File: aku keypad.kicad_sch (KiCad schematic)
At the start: 19 parts, among them J1 USB_C_Receptacle_USB2.0, SW1 SW_Push, SW2 MX_SW_HS, SW3 MX_SW_HS, U1 SRV05-4, U2 ATmega32U2-M, Y1 Crystal_GND24_Small

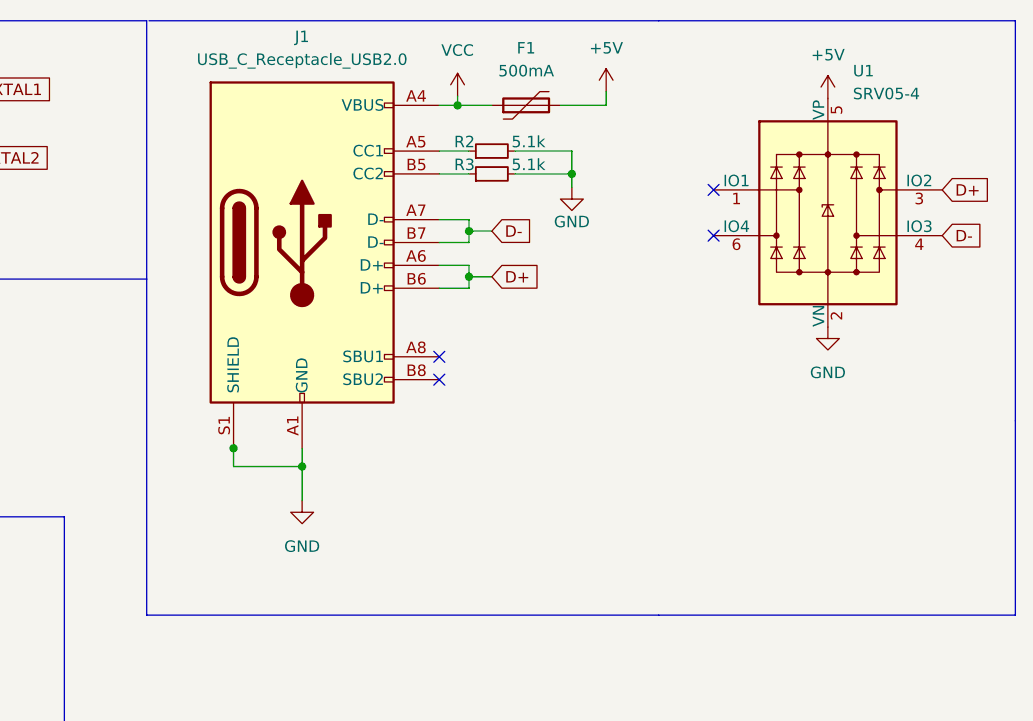
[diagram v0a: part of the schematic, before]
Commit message: redid routing on pcb
added type-c submodule, redid routing, changed usb components
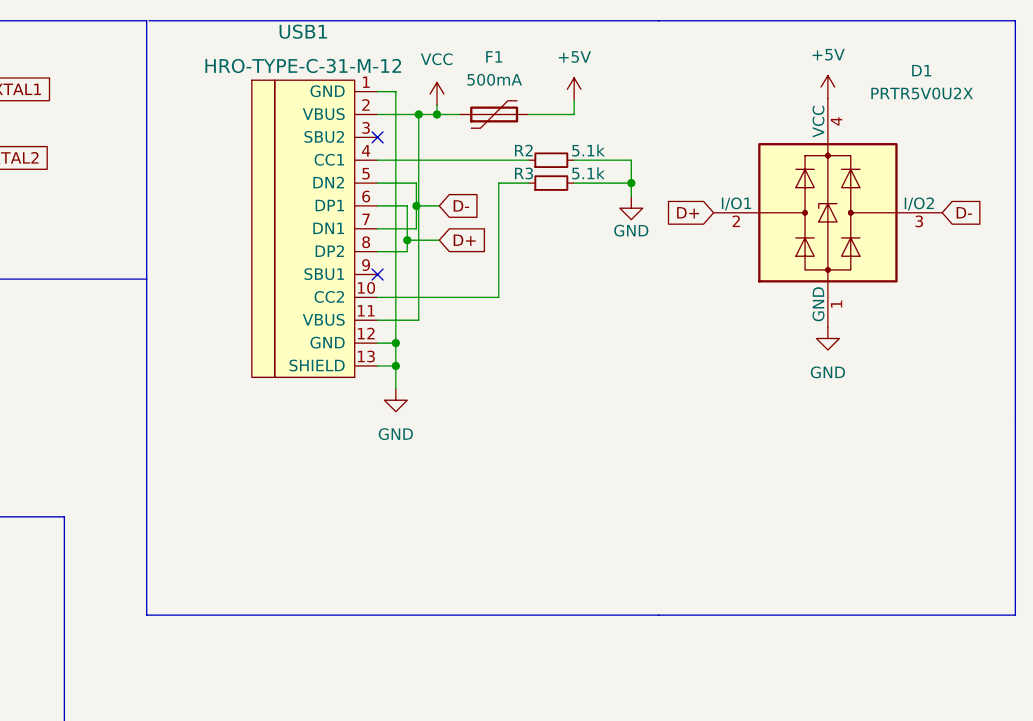
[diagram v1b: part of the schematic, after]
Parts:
- removed J1: USB_C_Receptacle_USB2.0, Connector_USB:USB_C_Receptacle_HRO_TYPE-C-31-M-12, symbol Connector:USB_C_Receptacle_USB2.0
- removed U1: SRV05-4, marbastlib-various:SOT-23-6-routable, symbol marbastlib-various:SRV05-4
- added D1: PRTR5V0U2X, Package_TO_SOT_SMD:SOT-143, symbol Power_Protection:PRTR5V0U2X
- added USB1: HRO-TYPE-C-31-M-12, Type-C:HRO-TYPE-C-31-M-12-HandSoldering, symbol Type-C:HRO-TYPE-C-31-M-12
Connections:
- net +5V: now also D1.4 (VCC)
- net D+: now also D1.2 (I/O1), USB1.6 (DP1), USB1.8 (DP2)
- net D-: now also D1.3 (I/O2), USB1.5 (DN2), USB1.7 (DN1)
- net GND: now also D1.1 (GND), USB1.1 (GND), USB1.12 (GND), USB1.13 (SHIELD)
- net VCC: now also USB1.11 (VBUS), USB1.2 (VBUS)
- net at R3.1: now also USB1.10 (CC2)
- net at R2.1: now also USB1.4 (CC1)
- no-connect marks 4 -> 2
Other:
- moved on the sheet: F1, R2, R3

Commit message: Added mounting holes
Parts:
- added H1, H2, H3, H4: MountingHole, random-keyboard-parts:Generic-Mounthole, symbol Mechanical:MountingHole
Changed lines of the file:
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@@
     (pin "2")
+  )
+  (symbol (lib_id "Mechanical:MountingHole") (at 213.106 103.886 0) (unit 1)
+    (in_bom yes) (on_board yes) (fields_autoplaced)
+    (property "Reference" "H1" (id 0) (at 215.9 102.6159 0)
+      (effects (font (size 1.27 1.27)) (justify left))
+    )
+    (property "Value" "MountingHole" (id 1) (at 215.9 105.1559 0)
+      (effects (font (size 1.27 1.27)) (justify left))
+    )
+    (property "Footprint" "random-keyboard-parts:Generic-Mounthole" (id 2) (at 213.106 103.886 0)
+      (effects (font (size 1.27 1.27)) hide)
+    )
+    (property "Datasheet" "~" (id 3) (at 213.106 103.886 0)
+      (effects (font (size 1.27 1.27)) hide)
+    )
   )
   (symbol (lib_id "Power_Protection:PRTR5V0U2X") (at 247.396 43.942 0) (unit 1)
@@
     (pin "1")
   )
+  (symbol (lib_id "Mechanical:MountingHole") (at 194.564 104.14 0) (unit 1)
+    (in_bom yes) (on_board yes) (fields_autoplaced)
+    (property "Reference" "H3" (id 0) (at 197.358 102.8699 0)
+      (effects (font (size 1.27 1.27)) (justify left))
+    )
+    (property "Value" "MountingHole" (id 1) (at 197.358 105.4099 0)
+      (effects (font (size 1.27 1.27)) (justify left))
+    )
+    (property "Footprint" "random-keyboard-parts:Generic-Mounthole" (id 2) (at 194.564 104.14 0)
+      (effects (font (size 1.27 1.27)) hide)
+    )
+    (property "Datasheet" "~" (id 3) (at 194.564 104.14 0)
+      (effects (font (size 1.27 1.27)) hide)
+    )
+  )
   (symbol (lib_id "Device:R_Small") (at 216.662 40.64 90) (unit 1)
     (in_bom yes) (on_board yes)
@@
     (pin "1")
     (pin "2")
+  )
+  (symbol (lib_id "Mechanical:MountingHole") (at 231.394 103.886 0) (unit 1)
+    (in_bom yes) (on_board yes) (fields_autoplaced)
+    (property "Reference" "H2" (id 0) (at 234.188 102.6159 0)
+      (effects (font (size 1.27 1.27)) (justify left))
+    )
+    (property "Value" "MountingHole" (id 1) (at 234.188 105.1559 0)
+      (effects (font (size 1.27 1.27)) (justify left))
+    )
+    (property "Footprint" "random-keyboard-parts:Generic-Mounthole" (id 2) (at 231.394 103.886 0)
+      (effects (font (size 1.27 1.27)) hide)
+    )
+    (property "Datasheet" "~" (id 3) (at 231.394 103.886 0)
+      (effects (font (size 1.27 1.27)) hide)
+    )
   )
   (symbol (lib_id "Device:C_Small") (at 127.762 37.846 90) (unit 1)
@@
     (pin "1")
   )
+  (symbol (lib_id "Mechanical:MountingHole") (at 175.006 104.648 0) (unit 1)
+    (in_bom yes) (on_board yes) (fields_autoplaced)
+    (property "Reference" "H4" (id 0) (at 177.8 103.3779 0)
+      (effects (font (size 1.27 1.27)) (justify left))
+    )
+    (property "Value" "MountingHole" (id 1) (at 177.8 105.9179 0)
+      (effects (font (size 1.27 1.27)) (justify left))
+    )
+    (property "Footprint" "random-keyboard-parts:Generic-Mounthole" (id 2) (at 175.006 104.648 0)
+      (effects (font (size 1.27 1.27)) hide)
+    )
+    (property "Datasheet" "~" (id 3) (at 175.006 104.648 0)
+      (effects (font (size 1.27 1.27)) hide)
+    )
+  )
   (symbol (lib_id "Device:R_Small") (at 40.132 34.036 0) (unit 1)
     (in_bom yes) (on_board yes)
@@
       (reference "F1") (unit 1) (value "500mA") (footprint "Fuse:Fuse_0402_1005Metric")
     )
+    (path "/118084c1-8298-4f2a-b210-24f333730244"
+      (reference "H1") (unit 1) (value "MountingHole") (footprint "random-keyboard-parts:Generic-Mounthole")
+    )
+    (path "/70560d5c-d51b-4b15-99ee-8f934bd88392"
+      (reference "H2") (unit 1) (value "MountingHole") (footprint "random-keyboard-parts:Generic-Mounthole")
+    )
+    (path "/3d5f794e-a9bc-4f6a-be1d-3c6917ebb555"
+      (reference "H3") (unit 1) (value "MountingHole") (footprint "random-keyboard-parts:Generic-Mounthole")
+    )
+    (path "/d1c99075-887c-414d-970c-8195012fdc45"
+      (reference "H4") (unit 1) (value "MountingHole") (footprint "random-keyboard-parts:Generic-Mounthole")
+    )
     (path "/d3c5df22-acb0-41d2-afae-268746a62cba"
